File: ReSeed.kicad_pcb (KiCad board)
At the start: 2 copper layers, 60.8 x 99.9 mm, 51 parts, among them CN1 EDGE_CONNECTOR, CN2 AUDIO_OUT, CN3 AUDIO_IN, CN4 DB9_MALE, Q1 BC549C, SW1 SW_DIGIFIX, U1 MOS_8580, U105 STEPUP_MT3608, U2 CD74HCT4520E, U3 74HCT245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

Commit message: Make counter reset DISABLABLE
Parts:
- added JP2: JMP_CNT_RST, Jumper:SolderJumper-3_P1.3mm_Open_RoundedPad1.0x1.5mm, B.Cu at (168.9, 121.5)
- moved V1 7.33 mm to (157.6, 97.2)
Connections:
- U2 pad 7: /reset -> Net-(JP2-Pad2)
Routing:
- net Net-(JP2-Pad2): track 0.00 -> 3.06 mm
- net GND: track 24.5 -> 25.6 mm
- net /reset: track 90.8 -> 90.5 mm, vias 1 -> 2
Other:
- board text added: "RST"
- board text added: "VIN+"
- board text added: "VIN-"
- board text added: "VOUT+"
- board text added: "VOUT-"

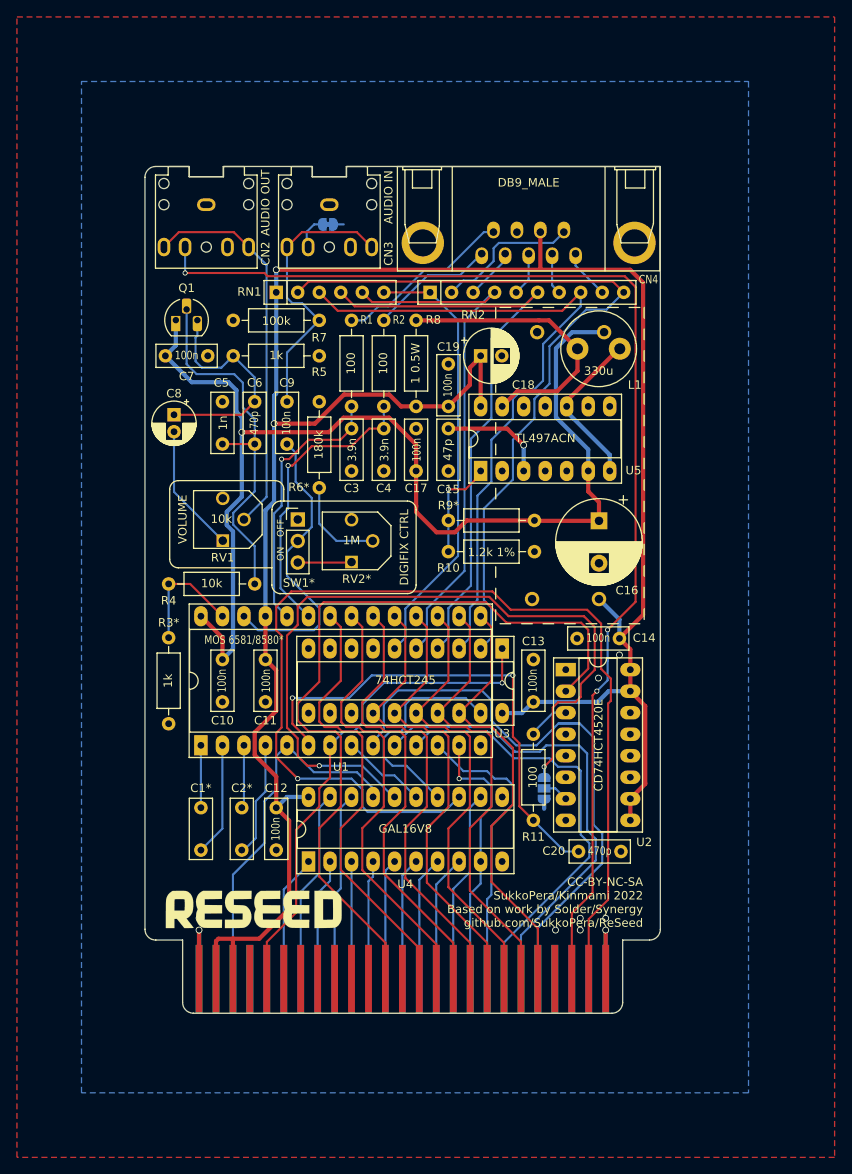
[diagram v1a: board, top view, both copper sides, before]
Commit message: Try separating signal and power grounds
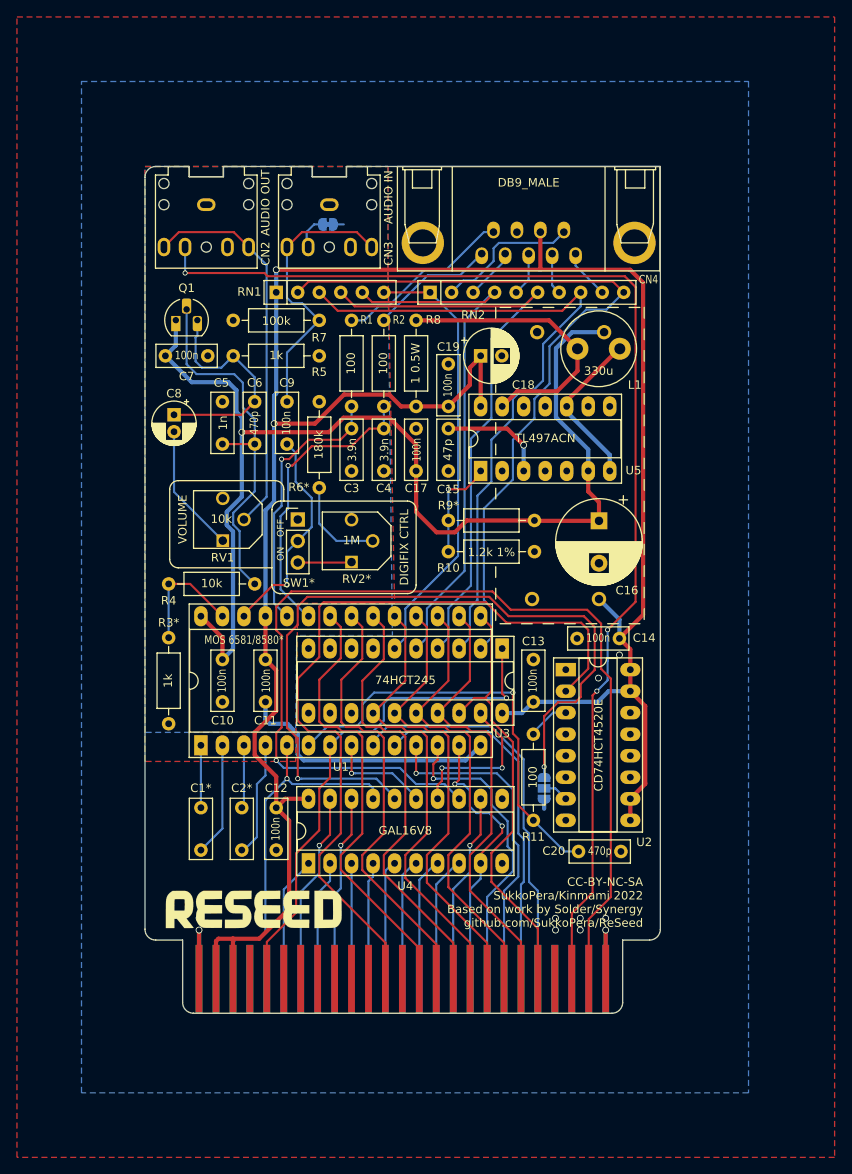
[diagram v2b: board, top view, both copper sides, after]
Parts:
- moved U4 0.21 mm to (141.1, 130.4)
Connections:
- C10 pad 2: GND -> GNDA
- C11 pad 2: GND -> GNDA
- C3 pad 2: GND -> GNDA
- C4 pad 2: GND -> GNDA
- C5 pad 2: GND -> GNDA
- C7 pad 1: GND -> GNDA
- CN2 pad S: GND -> GNDA
- CN3 pad S: GND -> GNDA
- JP1 pad 1: GND -> GNDA
- R3 pad 1: GND -> GNDA
- R5 pad 1: GND -> GNDA
- R6 pad 1: GND -> GNDA
- R7 pad 1: GND -> GNDA
- RV1 pad 3: GND -> GNDA
- U1 pad 14: GND -> GNDA
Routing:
- net GNDA: track 0.00 -> 33.5 mm
- net /a0: track 71.0 -> 47.2 mm
- net /a1: track 56.2 -> 42.8 mm
- net /a2: track 51.2 -> 38.8 mm, vias 0 -> 1
- net /audio_in: track 35.2 -> 25.8 mm, vias 0 -> 1
- net /sidclk: track 58.6 -> 50.8 mm, vias 2 -> 1
- net /~port: track 26.3 -> 18.5 mm, vias 0 -> 2
- net /phi2: track 128.6 -> 126.3 mm
- net /~sid: track 10.1 -> 12.1 mm, vias 0 -> 1
- net /r_~w: track 59.4 -> 61.0 mm
- net /reset: track 90.5 -> 92.1 mm
- net GND: track 25.6 -> 24.1 mm, vias 9 -> 10
- net /a3: track 35.0 -> 36.3 mm, vias 0 -> 1
- net /a4: track 31.9 -> 33.1 mm, vias 1 -> 2
- net /a14: track 22.9 -> 22.7 mm, vias 0 -> 1
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- added copper zone on B.Cu, net GNDA
- added copper zone on F.Cu, net GNDA

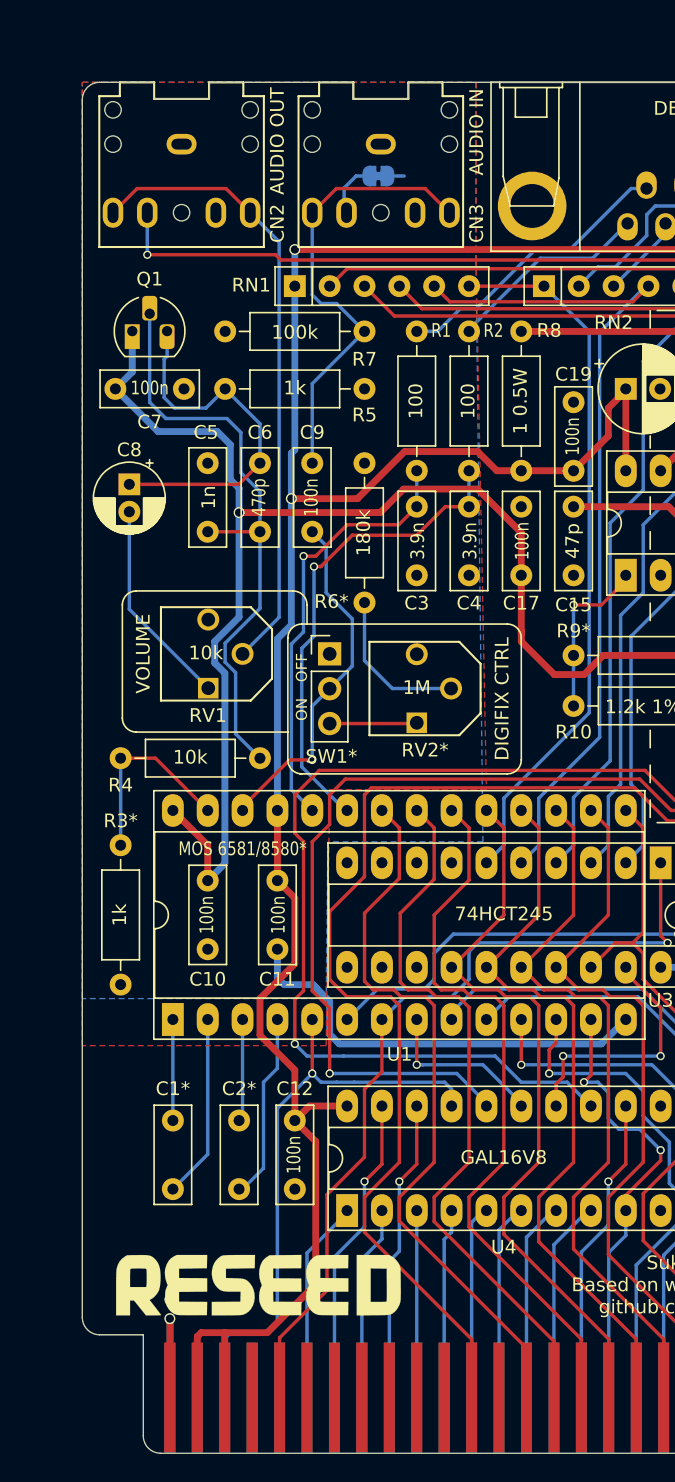
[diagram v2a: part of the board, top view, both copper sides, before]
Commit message: Only missing ferrites
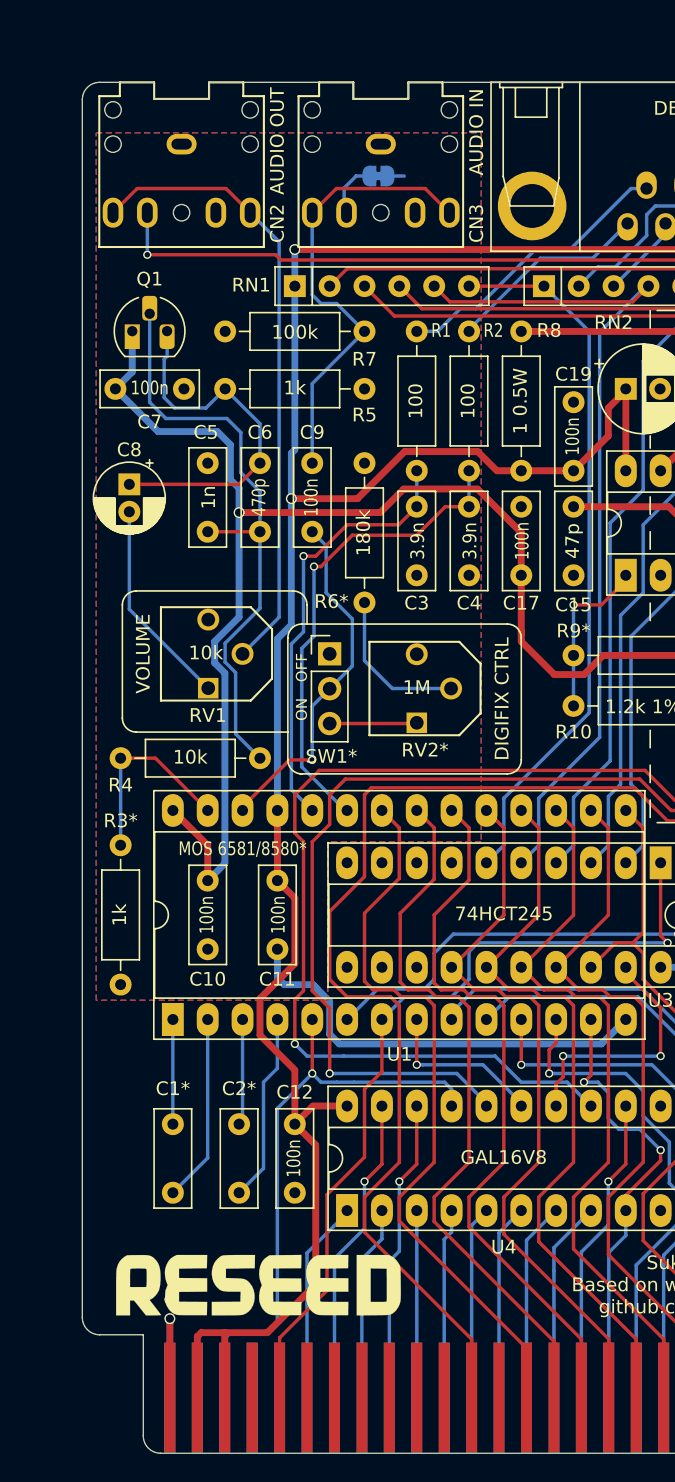
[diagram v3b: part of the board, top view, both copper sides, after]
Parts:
- moved C1 0.26 mm to (128.4, 124.1)
- moved C12 0.26 mm to (137.3, 124.1)
- moved C2 0.26 mm to (133.2, 124.1)
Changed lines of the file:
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@@
     (thickness 1.6)
     (drawings 110)
-    (tracks 670)
+    (tracks 675)
     (zones 0)
     (modules 52)
@@
   )
   (module Capacitor_THT:C_Disc_D7.0mm_W2.5mm_P5.00mm (layer F.Cu)
-    (at 128.397 123.825 270)
+    (at 128.397 124.089 270)
     (descr "C, Disc series, Radial, pin pitch=5.00mm, , diameter*width=7*2.5mm^2, Capacitor, http://cdn-reichelt.de/documents/datenblatt/B300/DS_KERKO_TC.pdf")
     (tags "C Disc series Radial pin pitch 5.00mm  diameter 7mm width 2.5mm Capacitor")
@@
   )
   (module Capacitor_THT:C_Disc_D7.0mm_W2.5mm_P5.00mm (layer F.Cu)
-    (at 133.223 123.825 270)
+    (at 133.223 124.089 270)
     (descr "C, Disc series, Radial, pin pitch=5.00mm, , diameter*width=7*2.5mm^2, Capacitor, http://cdn-reichelt.de/documents/datenblatt/B300/DS_KERKO_TC.pdf")
     (tags "C Disc series Radial pin pitch 5.00mm  diameter 7mm width 2.5mm Capacitor")
@@
   )
   (module Capacitor_THT:C_Disc_D7.0mm_W2.5mm_P5.00mm (layer F.Cu)
-    (at 137.287 123.825 270)
+    (at 137.287 124.089 270)
     (descr "C, Disc series, Radial, pin pitch=5.00mm, , diameter*width=7*2.5mm^2, Capacitor, http://cdn-reichelt.de/documents/datenblatt/B300/DS_KERKO_TC.pdf")
     (tags "C Disc series Radial pin pitch 5.00mm  diameter 7mm width 2.5mm Capacitor")
@@
   (gr_line (start 127.508 148.082) (end 176.911 148.082) (layer Edge.Cuts) (width 0.05))
   (segment (start 128.19 128.825) (end 128.143 128.778) (width 0.5) (layer F.Cu) (net 1) (status 30))
-  (segment (start 130.937 126.285) (end 128.397 128.825) (width 0.25) (layer B.Cu) (net 1) (status 20))
-  (segment (start 130.937 116.459) (end 130.937 126.285) (width 0.25) (layer B.Cu) (net 1) (status 10))
+  (segment (start 130.937 126.549) (end 128.397 129.089) (width 0.25) (layer B.Cu) (net 1))
+  (segment (start 130.937 116.459) (end 130.937 126.549) (width 0.25) (layer B.Cu) (net 1))
   (segment (start 128.397 116.459) (end 128.397 123.825) (width 0.25) (layer B.Cu) (net 2) (status 30))
   (segment (start 133.477 116.459) (end 133.477 123.825) (width 0.25) (layer B.Cu) (net 3) (status 30))
@@
   (segment (start 132.177 139.289) (end 130.463 139.289) (width 0.5) (layer F.Cu) (net 9))
   (segment (start 130.177 144.018) (end 130.177 139.575) (width 0.5) (layer F.Cu) (net 9) (status 10))
-  (segment (start 138.811 125.349) (end 137.287 123.825) (width 0.5) (layer F.Cu) (net 9) (status 20))
-  (segment (start 138.811 135.763) (end 138.811 125.349) (width 0.5) (layer F.Cu) (net 9))
   (segment (start 135.285 139.289) (end 138.811 135.763) (width 0.5) (layer F.Cu) (net 9))
   (segment (start 132.177 139.289) (end 135.285 139.289) (width 0.5) (layer F.Cu) (net 9))
@@
   (segment (start 177.8 101.604) (end 175.387 99.191) (width 0.5) (layer B.Cu) (net 9) (status 20))
   (segment (start 177.8 103.846) (end 177.8 101.604) (width 0.5) (layer B.Cu) (net 9) (status 10))
-  (segment (start 138.343 122.769) (end 137.287 123.825) (width 0.5) (layer F.Cu) (net 9) (status 20))
-  (segment (start 141.097 122.769) (end 138.343 122.769) (width 0.5) (layer F.Cu) (net 9) (status 10))
+  (segment (start 138.607 122.769) (end 137.287 124.089) (width 0.5) (layer F.Cu) (net 9))
+  (segment (start 141.097 122.769) (end 138.607 122.769) (width 0.5) (layer F.Cu) (net 9))
+  (segment (start 138.811 125.613) (end 137.287 124.089) (width 0.5) (layer F.Cu) (net 9))
+  (segment (start 138.811 128.397) (end 138.811 125.613) (width 0.5) (layer F.Cu) (net 9))
+  (segment (start 138.811 135.763) (end 138.811 128.397) (width 0.5) (layer F.Cu) (net 9))
   (segment (start 164.545 79.074) (end 166.497 81.026) (width 0.5) (layer F.Cu) (net 10))
   (segment (start 157.607 79.074) (end 164.545 79.074) (width 0.5) (layer F.Cu) (net 10) (status 10))
@@
   (segment (start 138.177 133.476) (end 141.097 130.556) (width 0.25) (layer B.Cu) (net 24) (status 20))
   (segment (start 138.177 144.018) (end 138.177 133.476) (width 0.25) (layer B.Cu) (net 24) (status 10))
-  (segment (start 140.177 133.762) (end 142.367 131.572) (width 0.25) (layer B.Cu) (net 25))
-  (segment (start 140.177 144.018) (end 140.177 133.762) (width 0.25) (layer B.Cu) (net 25) (status 10))
   (segment (start 143.637 127) (end 142.367 128.27) (width 0.25) (layer F.Cu) (net 25))
   (segment (start 143.637 122.769) (end 143.637 127) (width 0.25) (layer F.Cu) (net 25) (status 10))
   (via (at 142.367 128.27) (size 0.6) (drill 0.4) (layers F.Cu B.Cu) (net 25))
-  (segment (start 142.367 131.572) (end 142.367 128.27) (width 0.25) (layer B.Cu) (net 25))
+  (segment (start 142.367 131.699) (end 142.367 128.27) (width 0.25) (layer B.Cu) (net 25))
+  (segment (start 140.177 133.889) (end 142.367 131.699) (width 0.25) (layer B.Cu) (net 25))
+  (segment (start 140.177 144.018) (end 140.177 133.889) (width 0.25) (layer B.Cu) (net 25))
   (segment (start 143.637 132.461) (end 143.637 130.175) (width 0.25) (layer B.Cu) (net 26) (status 20))
   (segment (start 142.177 133.921) (end 143.637 132.461) (width 0.25) (layer B.Cu) (net 26))
@@
   (segment (start 148.717 131.953) (end 148.717 130.175) (width 0.25) (layer B.Cu) (net 29) (status 20))
   (segment (start 148.177 132.493) (end 148.717 131.953) (width 0.25) (layer B.Cu) (net 29))
-  (segment (start 150.177 131.255) (end 151.257 130.175) (width 0.25) (layer B.Cu) (net 30) (status 20))
-  (segment (start 150.177 144.018) (end 150.177 131.255) (width 0.25) (layer B.Cu) (net 30) (status 10))
-  (segment (start 152.177 131.795) (end 153.797 130.175) (width 0.25) (layer B.Cu) (net 31) (status 20))
-  (segment (start 152.177 144.018) (end 152.177 131.795) (width 0.25) (layer B.Cu) (net 31) (status 10))
-  (segment (start 154.177 132.335) (end 156.337 130.175) (width 0.25) (layer B.Cu) (net 32) (status 20))
-  (segment (start 154.177 144.018) (end 154.177 132.335) (width 0.25) (layer B.Cu) (net 32) (status 10))
-  (segment (start 156.177 132.875) (end 158.877 130.175) (width 0.25) (layer B.Cu) (net 33) (status 20))
-  (segment (start 156.177 144.018) (end 156.177 132.875) (width 0.25) (layer B.Cu) (net 33) (status 10))
+  (segment (start 150.177 131.469) (end 151.257 130.389) (width 0.25) (layer B.Cu) (net 30))
+  (segment (start 150.177 133.795) (end 150.177 131.469) (width 0.25) (layer B.Cu) (net 30))
+  (segment (start 150.177 144.018) (end 150.177 133.795) (width 0.25) (layer B.Cu) (net 30))
+  (segment (start 152.177 133.573) (end 152.177 132.009) (width 0.25) (layer B.Cu) (net 31))
+  (segment (start 152.177 144.018) (end 152.177 133.573) (width 0.25) (layer B.Cu) (net 31))
+  (segment (start 152.177 132.009) (end 153.797 130.389) (width 0.25) (layer B.Cu) (net 31))
+  (segment (start 154.177 132.549) (end 156.337 130.389) (width 0.25) (layer B.Cu) (net 32))
+  (segment (start 154.177 134.494) (end 154.177 132.549) (width 0.25) (layer B.Cu) (net 32))
+  (segment (start 154.177 144.018) (end 154.177 134.494) (width 0.25) (layer B.Cu) (net 32))
+  (segment (start 156.177 133.089) (end 158.877 130.389) (width 0.25) (layer B.Cu) (net 33))
+  (segment (start 156.177 134.78) (end 156.177 133.089) (width 0.25) (layer B.Cu) (net 33))
+  (segment (start 156.177 144.018) (end 156.177 134.78) (width 0.25) (layer B.Cu) (net 33))
   (segment (start 161.417 127) (end 160.147 128.27) (width 0.25) (layer F.Cu) (net 34))
   (segment (start 161.417 122.769) (end 161.417 127) (width 0.25) (layer F.Cu) (net 34) (status 10))
@@
   (segment (start 146.122 94.884) (end 146.177 94.829) (width 0.25) (layer B.Cu) (net 54) (status 30))
   (segment (start 139.827 94.884) (end 146.122 94.884) (width 0.25) (layer F.Cu) (net 54) (status 30))
-  (segment (start 135.001 127.301) (end 133.477 128.825) (width 0.25) (layer B.Cu) (net 55) (status 20))
-  (segment (start 135.001 121.031) (end 135.001 127.301) (width 0.25) (layer B.Cu) (net 55))
+  (segment (start 135.001 127.311) (end 133.223 129.089) (width 0.25) (layer B.Cu) (net 55))
+  (segment (start 135.001 121.031) (end 135.001 127.311) (width 0.25) (layer B.Cu) (net 55))
   (segment (start 136.017 120.015) (end 135.001 121.031) (width 0.25) (layer B.Cu) (net 55))
-  (segment (start 136.017 116.459) (end 136.017 120.015) (width 0.25) (layer B.Cu) (net 55) (status 10))
+  (segment (start 136.017 116.459) (end 136.017 120.015) (width 0.25) (layer B.Cu) (net 55))
   (segment (start 149.987 76.454) (end 149.987 79.074) (width 0.25) (layer B.Cu) (net 56) (status 30))
   (via (at 138.684 83.439) (size 0.6) (drill 0.4) (layers F.Cu B.Cu) (net 56))
@@
     )
   )
-  (zone (net 101) (net_name GNDA) (layer F.Cu) (hatch edge 0.508)
-    (priority 10)
-    (connect_pads (clearance 0.381))
-    (min_thickness 0.127)
-    (fill yes (arc_segments 32) (thermal_gap 0.254) (thermal_bridge_width 0.508) (smoothing fillet) (radius 2))
-    (polygon
-      (pts
-        (xy 150.495 61.087) (xy 151.257 99.695) (xy 139.827 99.695) (xy 139.573 118.364) (xy 121.793 118.364)
-        (xy 121.793 48.133) (xy 150.495 48.133)
-      )
-    )
-  )
   (zone (net 101) (net_name GNDA) (layer B.Cu) (hatch edge 0.508)
     (priority 10)
@@
     (polygon
       (pts
-        (xy 150.495 61.087) (xy 151.003 103.505) (xy 139.7 103.505) (xy 139.573 114.935) (xy 121.793 114.935)
-        (xy 121.793 48.133) (xy 150.495 48.133)
+        (xy 150.876 103.505) (xy 139.7 103.505) (xy 139.7 115.062) (xy 122.809 115.062) (xy 122.809 51.816)
+        (xy 150.876 51.816)
       )
     )
@@
       )
     )
+  )
+  (zone (net 101) (net_name GNDA) (layer F.Cu) (hatch edge 0.508)
+    (priority 10)
+    (connect_pads (clearance 0.381))
+    (min_thickness 0.127)
+    (fill yes (arc_segments 32) (thermal_gap 0.254) (thermal_bridge_width 0.508) (smoothing fillet) (radius 2))
+    (polygon
+      (pts
+        (xy 150.876 103.505) (xy 139.7 103.505) (xy 139.7 115.062) (xy 122.809 115.062) (xy 122.809 51.816)
+        (xy 150.876 51.816)
+      )
+    )
